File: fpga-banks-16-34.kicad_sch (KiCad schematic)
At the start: 25 parts, among them U1 ASFLMB-100.000MHZ-XY-T, U15 XC7K160T-FFG676, U8 PCA9517ADMR2G

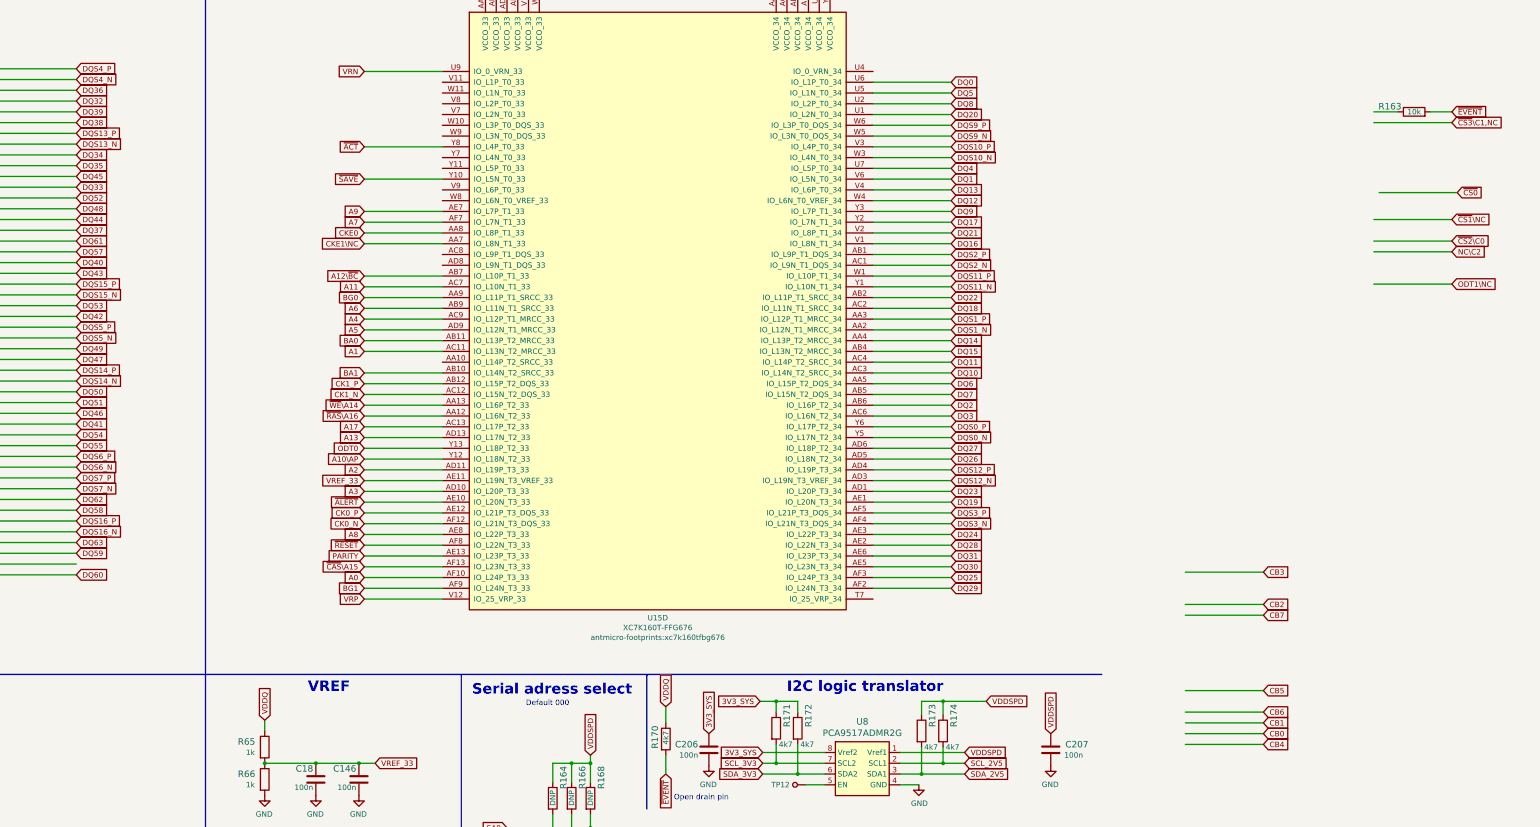
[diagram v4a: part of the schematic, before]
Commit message: Finish assigning address, command and control pins. Finish initial rerouting of DDR4 interface
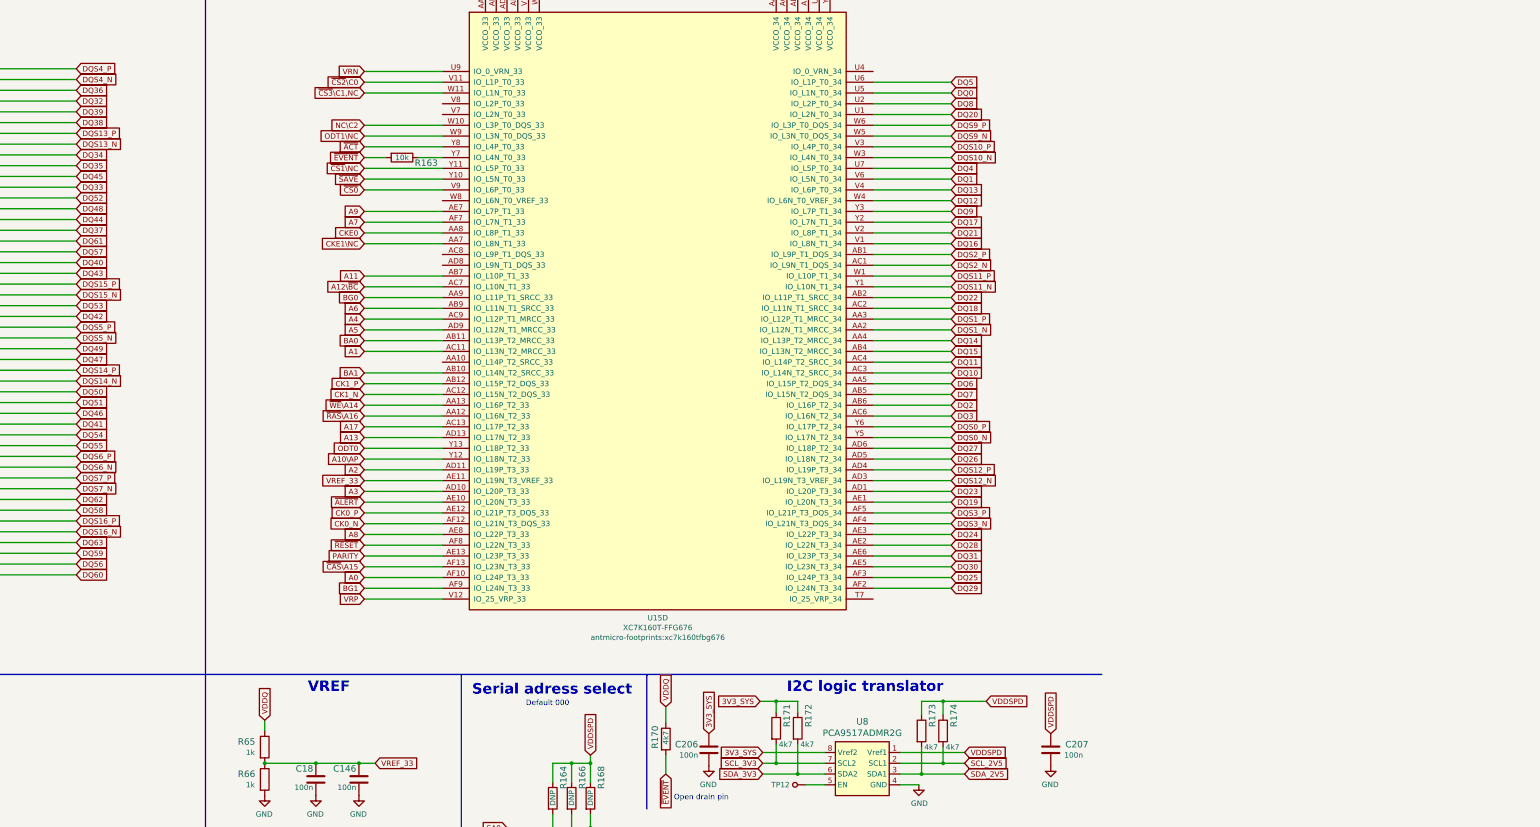
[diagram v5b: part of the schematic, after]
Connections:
- net A11: now also U15.AB7 (IO_L10P_T1_33); no longer U15.AC7 (IO_L10N_T1_33)
- net A12\~{BC}: now also U15.AC7 (IO_L10N_T1_33); no longer U15.AB7 (IO_L10P_T1_33)
- net DQ0: now also U15.U5 (IO_L1N_T0_34); no longer U15.U6 (IO_L1P_T0_34)
- net DQ5: now also U15.U6 (IO_L1P_T0_34); no longer U15.U5 (IO_L1N_T0_34)
- net NC\C2: now also U15.W10 (IO_L3P_T0_DQS_33)
- net ODT1\NC: now also U15.W9 (IO_L3N_T0_DQS_33)
- net ~{CS0}: now also U15.V9 (IO_L6P_T0_33)
- net ~{CS1}\NC: now also U15.Y11 (IO_L5P_T0_33)
- net ~{CS2}\C0: now also U15.V11 (IO_L1P_T0_33)
- net ~{CS3}\C1,NC: now also U15.W11 (IO_L1N_T0_33)
- net at R163.1: now also U15.Y7 (IO_L4N_T0_33)
- net DQ56: now reaches U15.V14 (IO_L24P_T3_32)
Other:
- moved on the sheet: R163

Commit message: Cleanup schematic
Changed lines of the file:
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@@
   (title_block
     (title "Data Center DRAM Tester")
-    (date "2022-09-07")
+    (date "2022-10-31")
     (rev "1.2.0")
     (company "Antmicro Ltd.")
@@
     (stroke (width 0) (type default) (color 0 0 0 0))
   )
-  (polyline (pts (xy 92.075 285.115) (xy 92.075 221.615))
-    (stroke (width 0) (type default) (color 0 0 0 0))
-  )
